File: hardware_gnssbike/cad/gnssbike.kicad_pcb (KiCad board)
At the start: 4 copper layers, 55 x 97 mm, 113 parts, among them J101 Molex 2036150003, J102 JST SM06B-GHS-TB, J201 Tag-Connect TC2030-NL, J401 Hirose FH28-10S-0.5SH, J402 Molex 503480-0500, Q401 DMG1012T-7, Q601 DMG1012T-7, Q602 DMG1012T-7, Q603 DMG1012T-7, SW601 Omron B3S-1002P, SW602 Omron B3S-1002P, SW603 Omron B3S-1002P, U101 nPM1300-QEAA, U102 MAX17262REWL, U103 AEM10900, U104 TPS7A0218PDQN, U201 MinewSemi ME54BS13, U301 u-blox MAX-F10S, U302 TI TXU0204BQAR, U501 MX25R6435F, U502 Bosch BMP585, U503 Bosch BMI270, U504 MMC5633NJL, U505 TI OPT3001DNPR

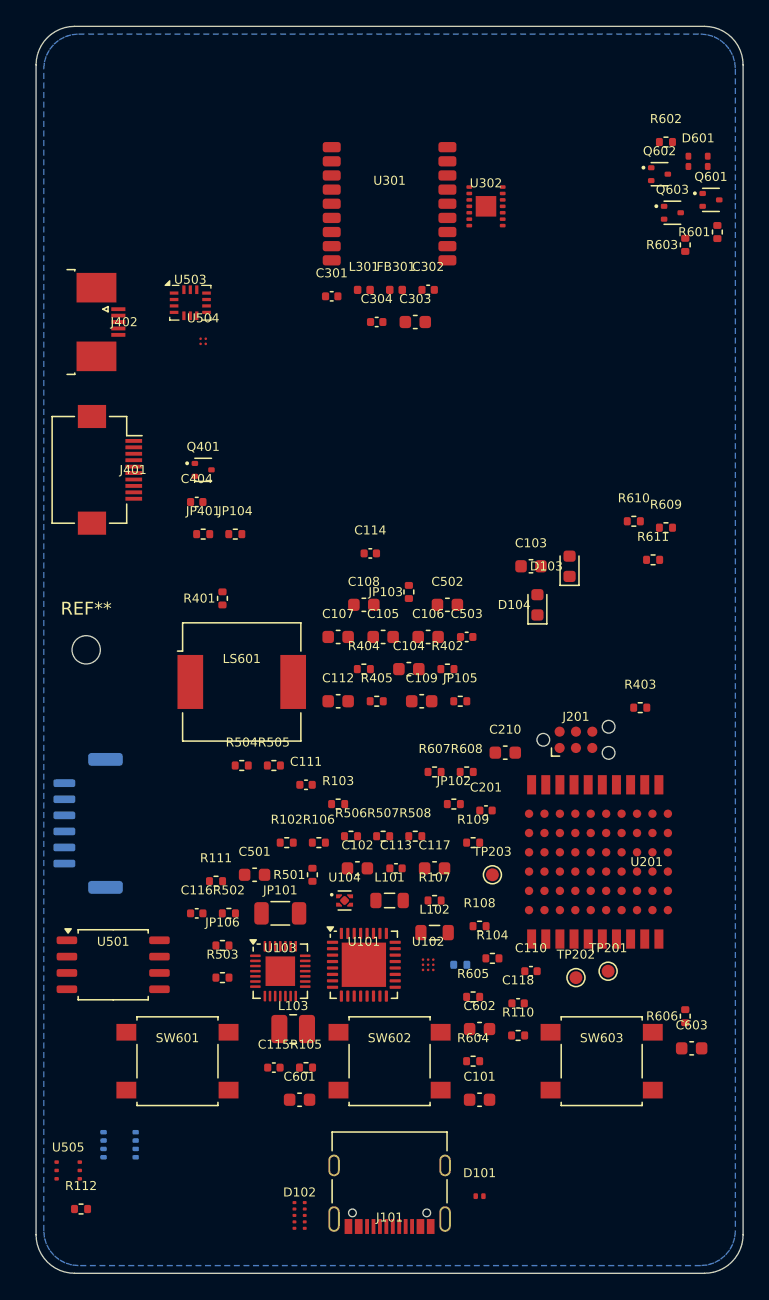
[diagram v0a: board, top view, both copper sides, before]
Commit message: feat(hardware): route the board without breaking a single design rule
Half of the board is routed and it passes: 90 of the 177 signal and power
connections, 524 segments, 250 vias, and zero DRC errors. The first version
of this router produced copper that failed 974 rules, so what follows is
what each of those was.

Two grids, not one. A track is 0.15 mm wide, a via is 0.45 with a 0.25 mm
hole, and a single grid inflated for the track put every via about 0.15 mm
too close to its neighbours. One grid says where a track may run, the other
where the CENTRE of a via may land.

Pads are rectangles, with their rotation applied, and a custom pad is read
from its primitives: the TPS7A02's anchor is 0.148 mm square while its
copper reaches 0.46 x 0.31, and reading the size alone left real copper
unguarded.

Clearance is no longer first come, first served. A cell inside TWO pads'
clearance used to remember one of them, and a track of that one then ran
0.025 mm from the other; a cell wanted by two nets now belongs to neither.

The classes come from gnssbike.kicad_pro instead of from memory - the USB
pair asks for 0.2 mm and was being given 0.127 - and a track necks down to
the pad it lands on, per connection, because a 0.4 mm rail on a 0.2 mm pad
sticks out on both sides.

A via is drilled where it was checked. It used to be checked at the grid
cell and drilled at the raw coordinate, half a step - 0.075 mm - away.

Routing is repeatable: the previous run's copper is removed first. Without
that, running it twice left 1576 segments where the router had drawn 534,
and the DRC reported 206 crossings that nothing had ever drawn.

Ground goes by plane. F.Cu now carries a pour as well, so a ground pad is
connected even where no via fits, and the edge is stitched with a via every
3.5 mm at worst - a tenth of a wavelength at 2.44 GHz is about 6 mm.
In2.Cu, which was an empty copper layer, became the third routing layer.

RF_IN and RF_ANT are deliberately left alone: 50 ohms needs the s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
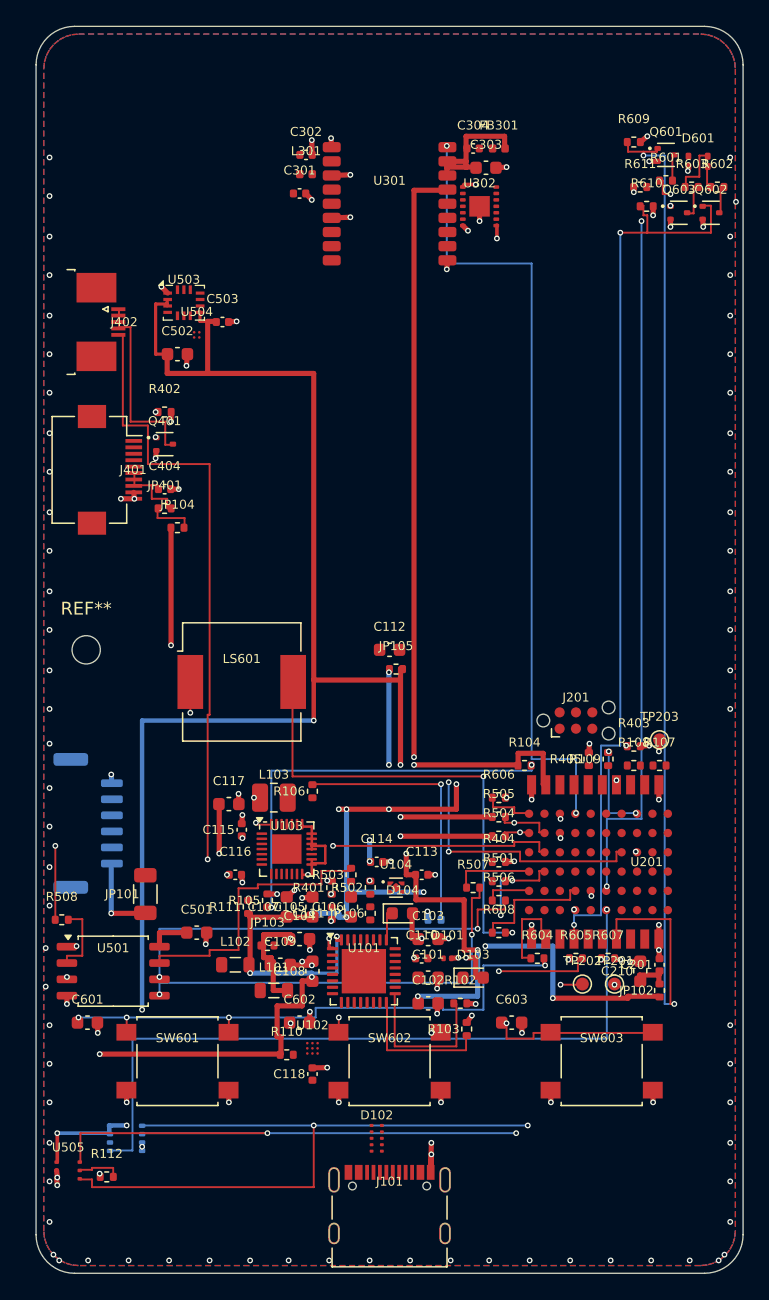
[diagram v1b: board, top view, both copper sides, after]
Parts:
- moved D103 32.9 mm to (59.0, 99.0), turned to 0 degrees
- moved C503 31.0 mm to (39.5, 48.0)
- moved R609 30.1 mm to (71.5, 34.0)
- moved C103 30.1 mm to (55.5, 96.0)
- moved R402 29.7 mm to (35.0, 55.0)
- moved JP103 29.6 mm to (43.0, 96.5), turned to 0 degrees
- moved R611 29.0 mm to (72.0, 37.5)
- moved C108 28.8 mm to (46.5, 98.5), turned to 90 degrees
- moved C502 28.7 mm to (36.0, 50.5)
- moved R508 28.3 mm to (27.0, 94.5)
- moved D104 26.2 mm to (53.5, 94.0), turned to 0 degrees
- moved R610 24.5 mm to (72.5, 39.0)
- moved R401 24.1 mm to (48.0, 92.0)
- moved C114 24.0 mm to (51.5, 90.0)
- moved C109 23.3 mm to (44.0, 98.0)
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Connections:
- C107 pad 2: (no net) -> GND
- C108 pad 2: (no net) -> GND
- C109 pad 2: (no net) -> GND
- C113 pad 2: (no net) -> GND
- C501 pad 1: SD3V0 -> SD3V0_FLASH
- L103 pad 1: SW_DCDC -> SRC
- L103 pad 2: SW_DCDC_L -> SW_DCDC
- R107 pad 2: 3V0 -> PWR_SDA
- U101 pad 13: 3V0 -> PWR_SDA
- U102 pad C1: 3V0 -> PWR_SDA
- U103 pad 13: 3V0 -> PWR_SDA
- U103 pad 8: SW_DCDC_L -> (no net)
- U201 pad B0: 3V0 -> PWR_SDA
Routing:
- net 3V0: track 0.00 -> 220.1 mm, vias 0 -> 19
- net 3V0_SENS: track 0.00 -> 143.0 mm, vias 0 -> 8
- net RGB_R: track 0.00 -> 84.6 mm, vias 0 -> 2
- net SENS_SCL: track 0.00 -> 82.5 mm, vias 0 -> 3
- net BL_PWM: track 0.00 -> 72.2 mm, vias 0 -> 4
- net SENS_SDA: track 0.00 -> 71.8 mm, vias 0 -> 3
- net RGB_G: track 0.00 -> 70.9 mm, vias 0 -> 2
- net GNSS_RESET_N: track 0.00 -> 62.1 mm, vias 0 -> 2
- net RGB_B: track 0.00 -> 60.3 mm, vias 0 -> 4
- net BL_ANODO: track 0.00 -> 59.2 mm, vias 0 -> 2
- net VBCKP: track 0.00 -> 58.2 mm, vias 0 -> 3
- net BARO_INT: track 0.00 -> 57.5 mm, vias 0 -> 1
- net GND: track 0.00 -> 56.9 mm, vias 0 -> 136
- net BUZ_A_LS: track 0.00 -> 55.6 mm, vias 0 -> 2
- net NOR_CS: track 0.00 -> 46.4 mm, vias 0 -> 3
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- added copper zone on F.Cu, net GND

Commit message: fix(hardware): the antenna rules are the ones the datasheet really writes
This file carried a rule that does not exist. It said "20 mm between the
module's antenna and any switching converter or inductor, datasheet 7.3", and
the ME54BS13 datasheet V1.0.0 says no such thing. Reading it instead of a
summary of it:

  7.3  no copper pour, no component and no fully enclosed metal housing over
       the antenna area, and the RF side never faces inward;
  7.4  the module at the edge or a corner, "no signal traces, metal objects,
       or other interference sources within 3-5 mm around the antenna area",
       and the PCB beneath the antenna HOLLOWED OUT so it hangs free;
  7.2  the decoupling capacitor 0.5 mm from the power pin, not 2 mm, and a
       pi filter footprint reserved because the supply is switching.

The invented rule was not merely useless. While it held the power supply
20 mm away, ten other parts sat within 5 mm of the antenna, one of them at
0.8 mm, and nothing complained - it was measuring the wrong thing rigorously.

The u-blox rules were checked the same way, in MAX-F10S integration manual
UBXDOC-963802114-12892: 5 mm from the receiver to any RF component (4.4),
0.2 ohm maximum series resistance on VCC (4.1.1), ground under the module on
the first two layers, and coplanar waveguide for the RF line.

What changed on the board. The module moved from the middle of the right
edge to the bottom right CORNER, which is the arrangement figure 1 of 7.5
calls "Best", and the board now has a notch under its antenna:

  antennas 65.7 mm apart -> 84.9, which is 2.8 quarter waves at 2.44 GHz
  nearest foreign part to the antenna 0.8 mm -> 5.7
  board hollowed under the antenna: no -> yes

Its own decoupling is the one named exemption, and it has to be: 7.2 wants
0.5 mm from a power pin that is itself 2.1 mm from the antenna, so no point
satisfies both. C201 and C210 are listed by name and their distance printed.

The rest of the board followed. Memory, sensors an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
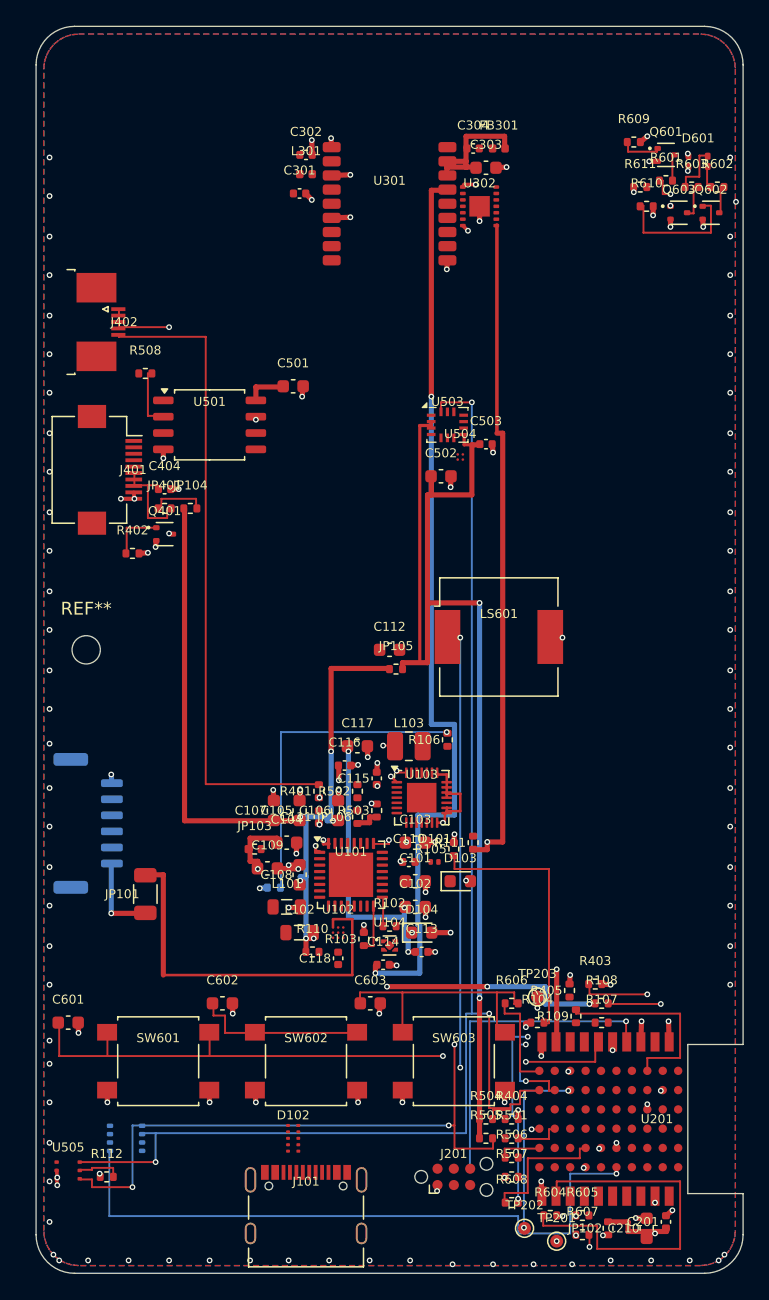
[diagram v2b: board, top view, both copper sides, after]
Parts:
- moved C501 43.2 mm to (45.0, 53.0)
- moved U501 43.2 mm to (38.5, 56.0)
- moved R508 43.0 mm to (33.5, 52.0)
- moved J201 36.7 mm to (57.5, 114.5)
- moved R505 25.0 mm to (60.0, 111.5)
- moved R507 22.7 mm to (62.0, 114.5)
- moved C502 22.6 mm to (56.5, 60.0)
- moved C503 22.6 mm to (60.0, 57.5)
- moved U503 22.6 mm to (57.0, 56.0)
- moved U504 22.6 mm to (58.0, 58.5)
- moved TP203 22.1 mm to (64.0, 100.5)
- moved R504 22.0 mm to (60.0, 110.0)
- moved R607 21.6 mm to (67.5, 119.0)
- moved R608 21.0 mm to (62.0, 116.5)
- moved R107 20.5 mm to (69.0, 102.5)
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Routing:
- net RGB_R: track 84.6 -> 3.30 mm, vias 2 -> 0
- net 3V0: track 220.1 -> 300.8 mm, vias 19 -> 15
- net VSYS: track 10.5 -> 86.2 mm, vias 2 -> 4
- net BL_PWM: track 72.2 -> 4.20 mm, vias 4 -> 0
- net GNSS_RESET_N: track 62.1 -> 0.00 mm, vias 2 -> 0
- net RGB_G: track 70.9 -> 10.3 mm, vias 2 -> 0
- net 3V0_SENS: track 143.0 -> 91.8 mm, vias 8 -> 2
- net NOR_MISO: track 44.8 -> 0.00 mm, vias 2 -> 0
- net NOR_CS: track 46.4 -> 3.60 mm, vias 3 -> 0
- net SENS_SDA: track 71.8 -> 110.0 mm
- net NOR_MOSI_F: track 33.3 -> 0.00 mm, vias 2 -> 0
- net NOR_SCK_F: track 33.0 -> 0.00 mm, vias 2 -> 0
- net NOR_WP: track 31.2 -> 0.00 mm, vias 2 -> 0
- net VBAT: track 0.00 -> 30.3 mm
- net KEY_C_SW: track 38.1 -> 13.5 mm, vias 4 -> 0
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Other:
- outline, holes or cut-outs redrawn

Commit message: feat(hardware): a 50 x 86 mm board, laid out from what decides its size
The board was 55 x 97 mm because a document written before any footprint
existed said so. Measured instead, from the parts that actually constrain it:

  width  = 0.8 edge + 7.9 display connector + 40.08 panel + 0.8 = 49.58
  height = 8.0 GNSS antenna zone + 61.8 display (starting at y 5.1)
           + 7.4 keys + 8.93 USB-C + 1.6 = 84.83

So 50 x 86: 4300 mm2 against 5335, 19 % less, and the parts go from filling
27.5 % of it to 34.1 %. What sets the size is the display and its connector,
not the electronics - the 1467 mm2 of courtyard would fit in 57 x 57.

The floorplan was laid out again rather than scaled down. The radio module
keeps the bottom right corner with its antenna over a notch; the keys sit
below the display and left of the antenna's clear band; memory, sensors and
the buzzer fill the band under the display; the power block takes the width
the module left. Every rule of the two datasheets still passes, and the DRC
reports no error.

Two things had to move for the module's own decoupling. Against the bottom
edge there was no room at all for it: the 0603 bulk capacitor's courtyard ran
past the 0.8 mm border margin and it was pushed 11.2 mm away, behind parts
with no such rule. The module moved up 3.5 mm, and the placer now hands out
the ring around a chip by how tight its rule is rather than by capacitance
alone, so the part with a 0.5 mm limit picks before the one with 5 mm.

Routing follows the GNSS reference design: section 4.4 of the MAX-F10S
integration manual asks for ground under the module on the first two layers
with no signal crossing beneath, and the router now refuses the front layer
there. In1.Cu was already solid ground.

Every drawn body got the colour and the shape of the real package instead of
one grey box for all of them: black epoxy for moulded ICs, tin plate for a
shield can, stainless for the USB-C shell with its black tongue, ivory for an
FPC housing, bare sil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
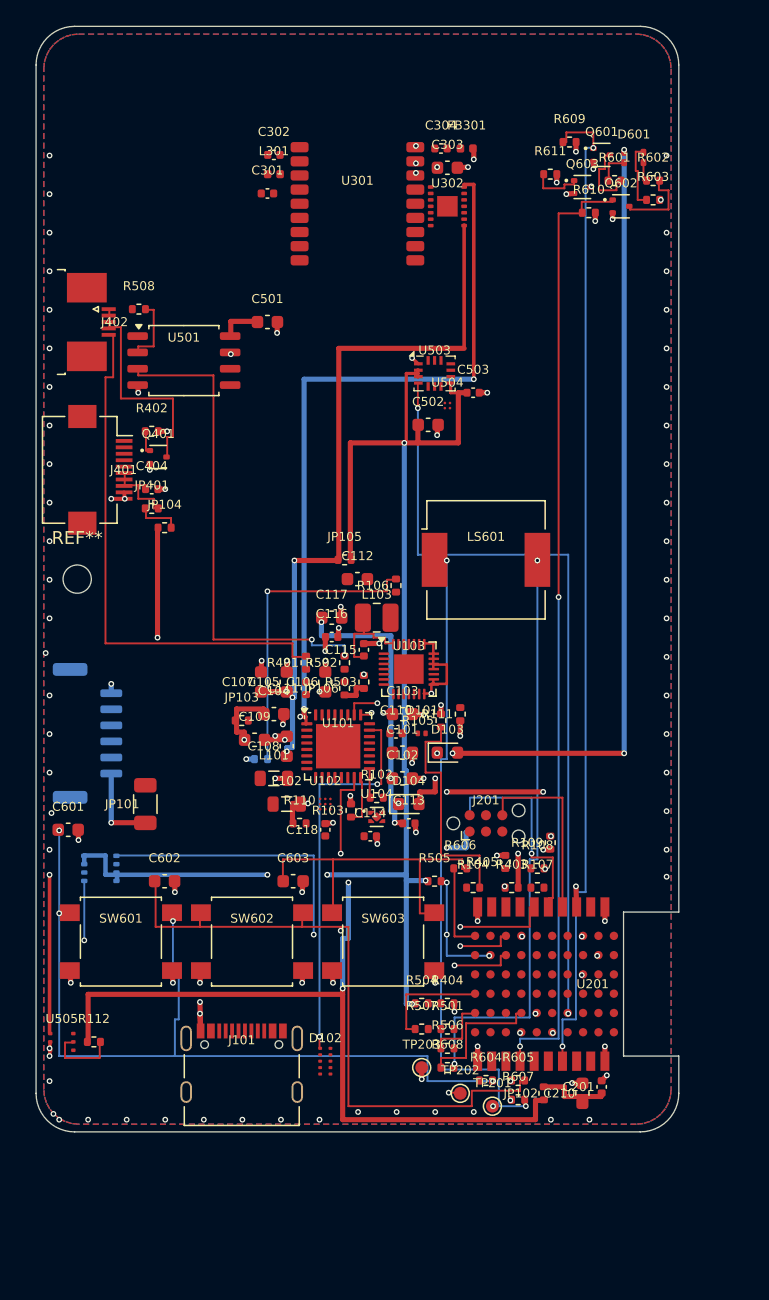
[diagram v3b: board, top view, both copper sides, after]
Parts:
- moved J201 27.6 mm to (60.0, 87.0)
- moved U502 21.1 mm to (30.0, 90.5)
- moved R505 20.4 mm to (56.0, 91.5)
- moved C601 15.0 mm to (27.5, 87.5)
- moved R109 13.6 mm to (65.0, 88.5)
- moved R507 13.5 mm to (55.0, 103.0)
- moved R106 12.6 mm to (53.0, 68.5)
- moved J101 12.1 mm to (41.0, 105.7)
- moved C201 11.6 mm to (69.0, 107.5)
- moved C210 11.6 mm to (67.5, 108.0)
- moved JP102 11.6 mm to (64.5, 108.0)
- moved R104 11.6 mm to (59.0, 92.0)
- moved R107 11.6 mm to (64.0, 92.0)
- moved R108 11.6 mm to (64.0, 90.5)
- moved R604 11.6 mm to (60.0, 107.0)
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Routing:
- net SENS_SDA: track 110.0 -> 0.00 mm, vias 3 -> 0
- net 3V0: track 300.8 -> 203.8 mm, vias 15 -> 14
- net RGB_B: track 79.0 -> 4.05 mm, vias 3 -> 0
- net RGB_R: track 3.30 -> 77.8 mm, vias 0 -> 2
- net GNSS_RESET_N: track 0.00 -> 71.4 mm, vias 0 -> 2
- net VBCKP: track 71.1 -> 0.00 mm, vias 2 -> 0
- net RGB_G: track 10.3 -> 74.2 mm, vias 0 -> 2
- net IMU_INT: track 0.00 -> 60.8 mm, vias 0 -> 2
- net 1V8: track 18.1 -> 74.0 mm, vias 3 -> 5
- net KEY_C_SW: track 13.5 -> 63.4 mm, vias 0 -> 2
- net 3V0_SENS: track 91.8 -> 134.9 mm, vias 2 -> 6
- net NOR_WP: track 0.00 -> 38.4 mm, vias 0 -> 2
- net VBUSOUT: track 38.1 -> 0.00 mm, vias 3 -> 0
- net CC1: track 0.00 -> 30.5 mm, vias 0 -> 2
- net VBAT: track 30.3 -> 0.00 mm
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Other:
- board size 55 x 97 mm -> 50 x 86 mm
